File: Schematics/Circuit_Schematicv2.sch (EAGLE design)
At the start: 73 parts, among them Q2 LE33CZ

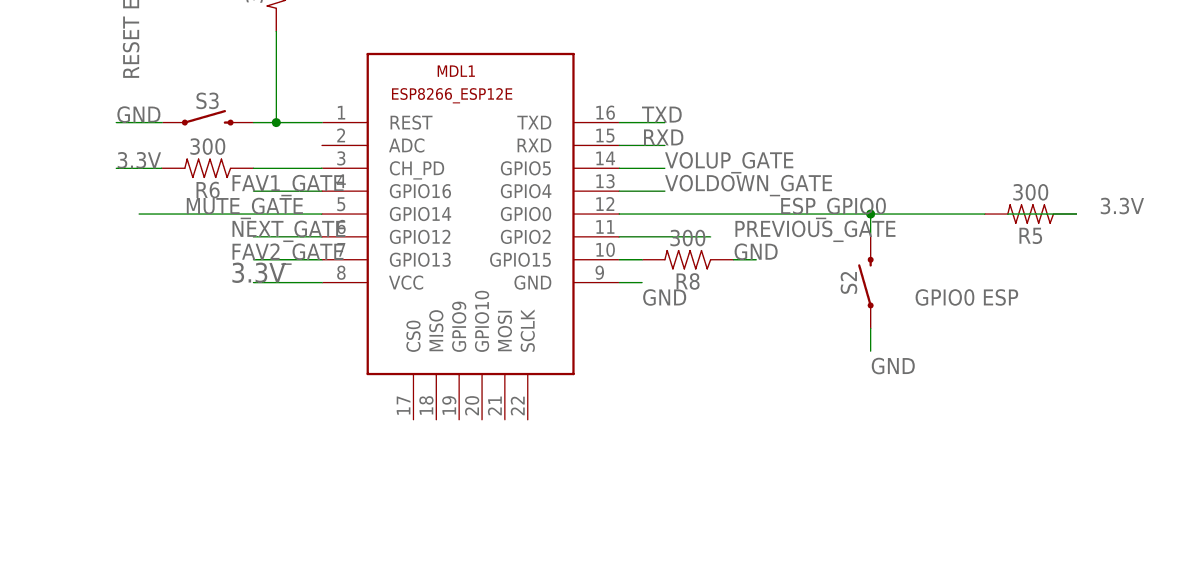
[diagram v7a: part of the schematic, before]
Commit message: Added GPIO jumpers instead of switches
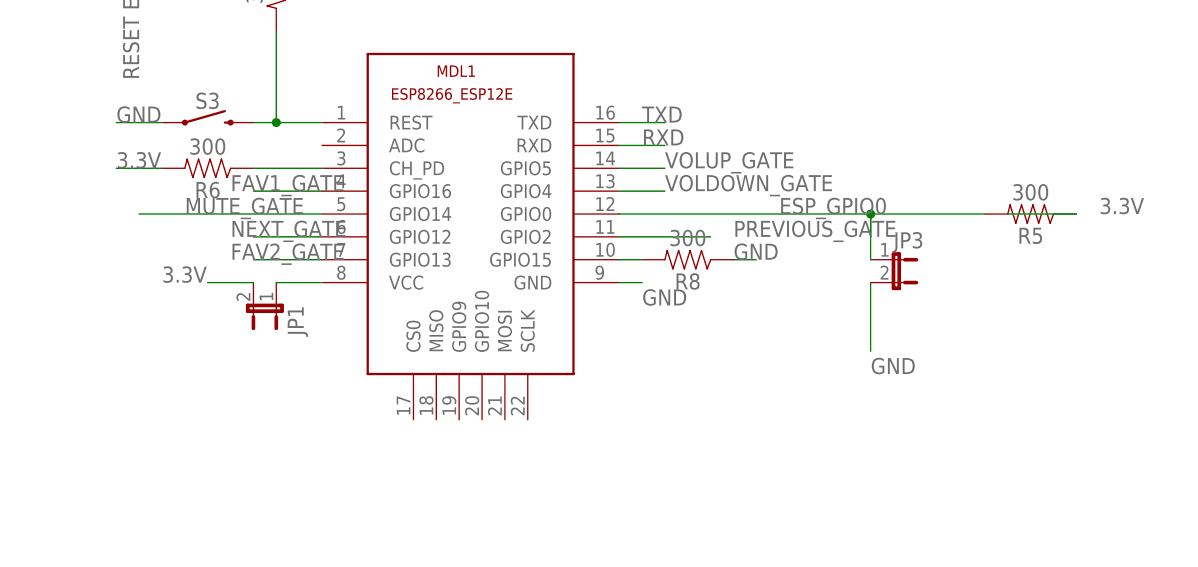
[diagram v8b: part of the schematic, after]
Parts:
- removed S2: GPIO0 ESP, SparkFun-Switches:MOMENTARY-SWITCH-SPST-SMD-6.0X3.5MM
- added JP1, JP3: (no value), jumper:JP1E
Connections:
- new net ESP_VCC: JP1.1, MDL1.VCC
- net 3.3V: now also JP1.2; no longer MDL1.VCC
- net ESP_GPIO0: now also JP3.1; no longer S2.2
- net GND: now also JP3.2; no longer S2.1
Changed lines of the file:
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@@
 <?xml version="1.0" encoding="utf-8"?>
 <!DOCTYPE eagle SYSTEM "eagle.dtd">
-<eagle version="8.1.0">
+<eagle version="8.0.0">
 <drawing>
 <settings>
@@
 <part name="R15" library="SparkFun-Resistors" deviceset="10KOHM" device="-0603-1/10W-1%" value="10k"/>
 <part name="R5" library="SparkFun-Resistors" deviceset="1OHM" device="-0603-1/10W-1%" value="300"/>
-<part name="S2" library="SparkFun-Switches" deviceset="MOMENTARY-SWITCH-SPST" device="-SMD-6.0X3.5MM" value="GPIO0 ESP"/>
 <part name="JP2" library="MIRO" deviceset="LCD16X2HEADER" device=""/>
 <part name="VR3" library="SparkFun-Resistors" deviceset="TRIMPOT" device="-SMD-3MM-OPEN-1/10W-25%" value="10k"/>
@@
 <part name="T6" library="zetex" deviceset="NMOSSOT223" device=""/>
 <part name="T7" library="zetex" deviceset="NMOSSOT223" device=""/>
+<part name="JP1" library="jumper" deviceset="JP1E" device=""/>
+<part name="JP3" library="jumper" deviceset="JP1E" device=""/>
 </parts>
 <sheets>
@@
 <instance part="R15" gate="G$1" x="426.72" y="195.58" rot="R270"/>
 <instance part="R5" gate="G$1" x="449.58" y="53.34" rot="R180"/>
-<instance part="S2" gate="G$1" x="431.8" y="45.72" smashed="yes" rot="R90">
-<attribute name="NAME" x="430.276" y="45.72" size="1.778" layer="95" font="vector" rot="R90" align="bottom-center"/>
-<attribute name="VALUE" x="442.468" y="43.18" size="1.778" layer="96" font="vector" rot="R180" align="top-center"/>
-</instance>
 <instance part="JP2" gate="A" x="5.08" y="-27.94" rot="R180"/>
 <instance part="VR3" gate="R?" x="38.1" y="-20.32" rot="R90"/>
@@
 <instance part="T6" gate="A" x="439.42" y="180.34"/>
 <instance part="T7" gate="A" x="464.82" y="180.34"/>
+<instance part="JP1" gate="A" x="365.76" y="43.18" rot="R180"/>
+<instance part="JP3" gate="A" x="434.34" y="48.26" rot="R270"/>
 </instances>
 <busses>
@@
 </segment>
 <segment>
-<pinref part="S2" gate="G$1" pin="1"/>
-<wire x1="431.8" y1="40.64" x2="431.8" y2="38.1" width="0.1524" layer="91"/>
 <label x="431.8" y="35.56" size="1.778" layer="95"/>
+<pinref part="JP3" gate="A" pin="2"/>
+<wire x1="431.8" y1="45.72" x2="431.8" y2="38.1" width="0.1524" layer="91"/>
 </segment>
 <segment>
@@
 <wire x1="111.76" y1="187.96" x2="116.84" y2="187.96" width="0.1524" layer="91"/>
 <label x="119.38" y="187.96" size="1.778" layer="95"/>
-</segment>
-<segment>
-<pinref part="MDL1" gate="G$1" pin="VCC"/>
-<wire x1="370.84" y1="45.72" x2="363.22" y2="45.72" width="0.1524" layer="91"/>
-<label x="360.68" y="45.72" size="2.1844" layer="95"/>
 </segment>
 <segment>
@@
 <label x="193.04" y="111.76" size="1.778" layer="95"/>
 </segment>
+<segment>
+<pinref part="JP1" gate="A" pin="2"/>
+<wire x1="363.22" y1="45.72" x2="358.14" y2="45.72" width="0.1524" layer="91"/>
+<label x="353.06" y="45.72" size="1.778" layer="95"/>
+</segment>
 </net>
 <net name="L-OUT" class="0">
@@
 <pinref part="R5" gate="G$1" pin="2"/>
 <wire x1="403.86" y1="53.34" x2="431.8" y2="53.34" width="0.1524" layer="91"/>
-<pinref part="S2" gate="G$1" pin="2"/>
 <wire x1="431.8" y1="53.34" x2="444.5" y2="53.34" width="0.1524" layer="91"/>
 <wire x1="431.8" y1="50.8" x2="431.8" y2="53.34" width="0.1524" layer="91"/>
 <junction x="431.8" y="53.34"/>
 <label x="421.64" y="53.34" size="1.778" layer="95"/>
-</segment>
-</net>
+<pinref part="JP3" gate="A" pin="1"/>
+<wire x1="431.8" y1="48.26" x2="431.8" y2="53.34" width="0.1524" layer="91"/>
+</segment>
+</net>
+<net name="ESP_VCC" class="0">
+<segment>
+<pinref part="MDL1" gate="G$1" pin="VCC"/>
+<pinref part="JP1" gate="A" pin="1"/>
+<wire x1="370.84" y1="45.72" x2="365.76" y2="45.72" width="0.1524" layer="91"/>
+</segment>
+</net>
